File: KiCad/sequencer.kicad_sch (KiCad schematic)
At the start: 19 parts, among them J1 GATE OUT, J2 GATE OUT, J3 GATE OUT, Q1 BC548, U1 TL074

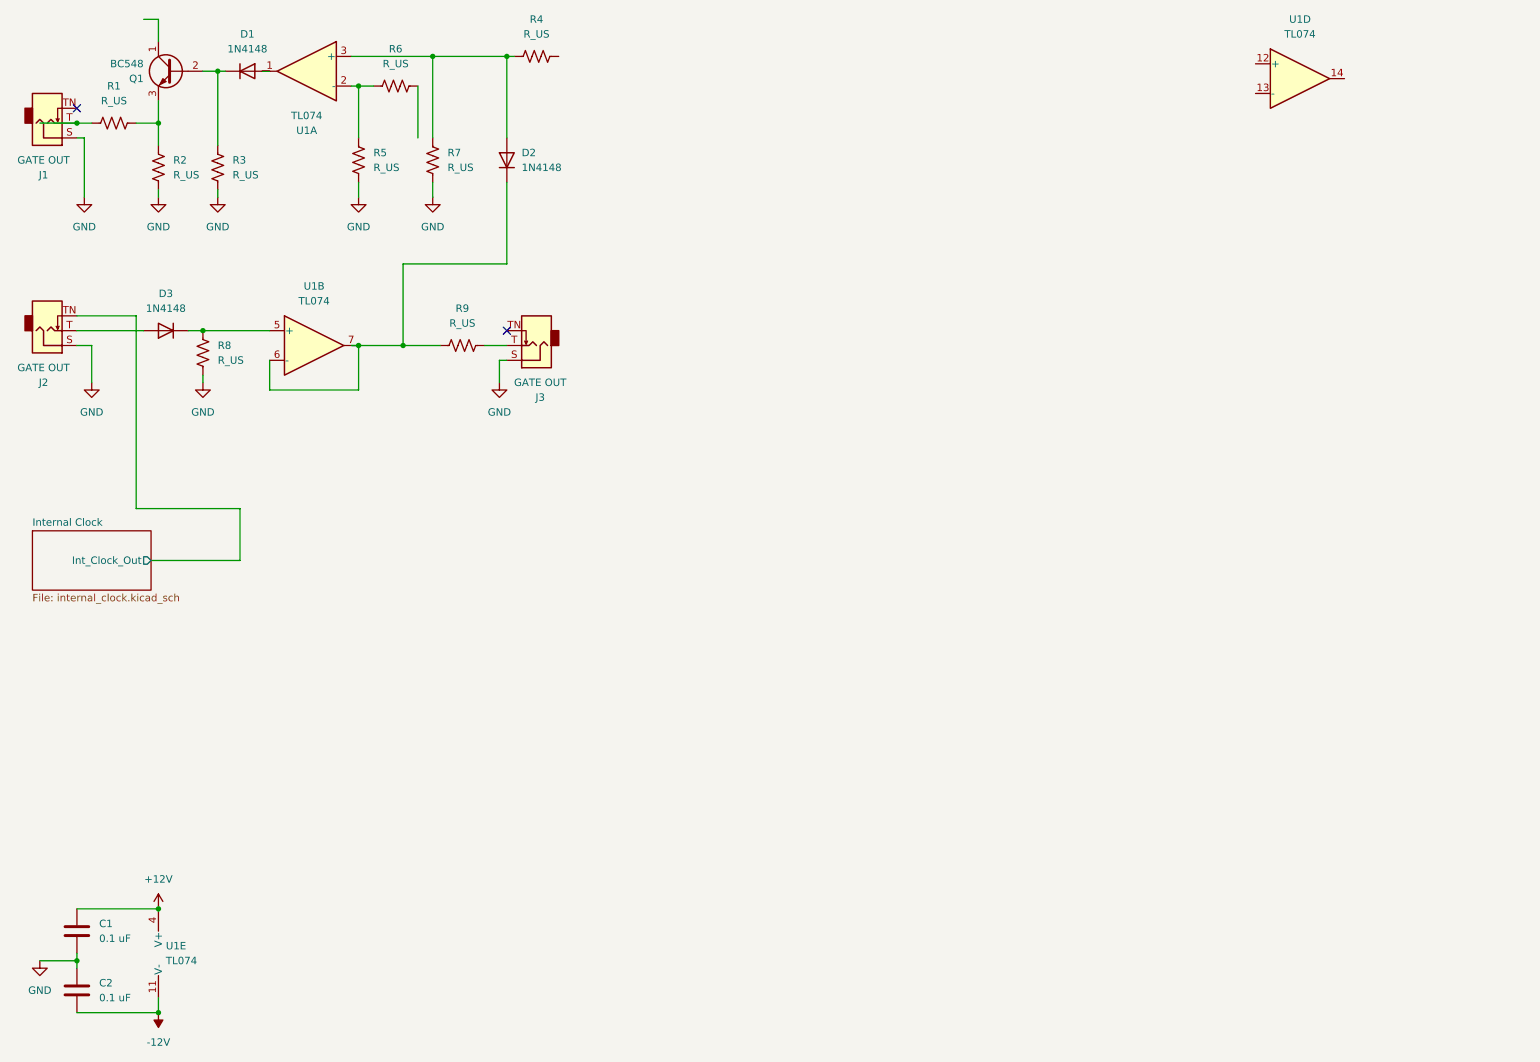
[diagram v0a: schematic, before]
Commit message: schematic: update cicada schematic
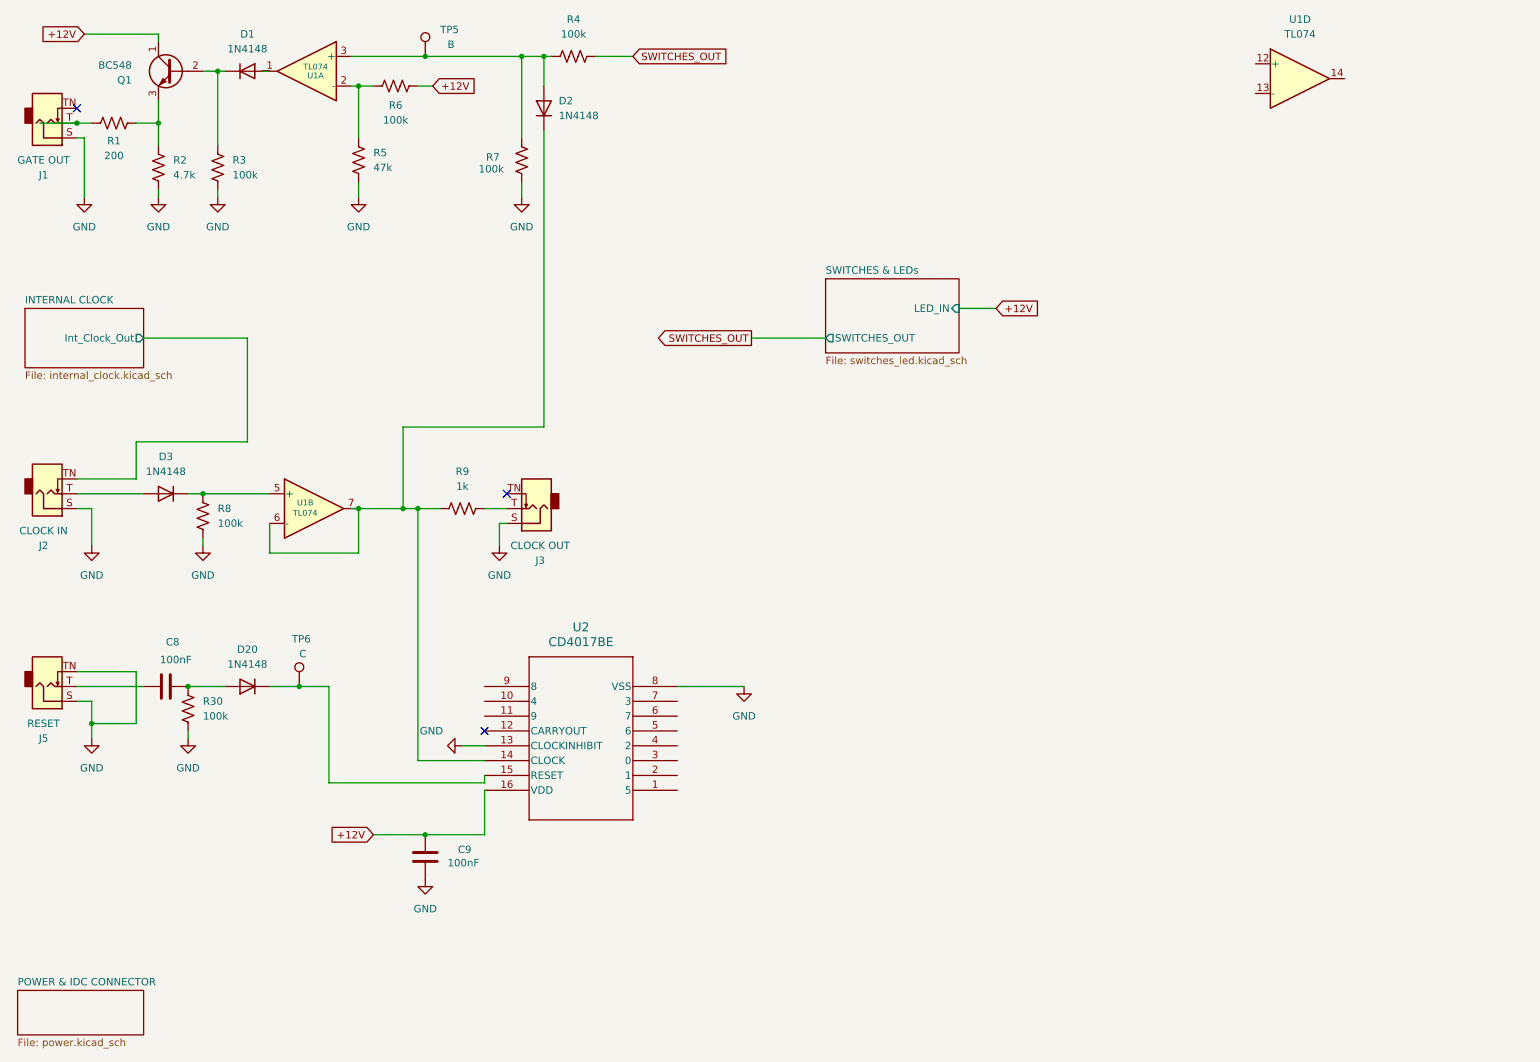
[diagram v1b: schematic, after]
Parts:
- removed C1, C2: 0.1 uF, symbol Device:C
- removed unit 5 of U1
- added C8, C9: 100nF, Capacitor_SMD:C_0805_2012Metric_Pad1.18x1.45mm_HandSolder, symbol Device:C
- added D20: 1N4148, Diode_THT:D_DO-35_SOD27_P7.62mm_Horizontal, symbol Diode:1N4148
- added J5: RESET, symbol Connector_Audio:AudioJack2_SwitchT
- added R30: 100k, symbol Device:R_US
- added TP5: B, symbol Connector:TestPoint
- added TP6: C, symbol Connector:TestPoint
- added U2: CD4017BE, N16, symbol Eurorack:CD4017BE
- J2: value GATE OUT -> CLOCK IN
- J3: value GATE OUT -> CLOCK OUT
- R1: value R_US -> 200
- R2: value R_US -> 4.7k
- R3, R4, R6, R7, R8: value R_US -> 100k
- R5: value R_US -> 47k
- R9: value R_US -> 1k
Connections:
- net +12V: now also Q1.1 (C), R6.1, C9.1, U2.16 (VDD)
- net GND: now also C9.2, J5.S, J5.TN, R30.1, U2.13 (CLOCKINHIBIT), U2.8 (VSS)
- net at D2.2 (A), R4.2, R7.2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: now also TP5.1
- net at D2.1 (K), R9.2, U1.6 (-)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: now also U2.14 (CLOCK)
- net SWITCHES_OUT: now reaches R4.1
- new net: D20.1 (K), TP6.1, U2.15 (RESET)
- new net: C8.1, D20.2 (A), R30.2
- new net: C8.2, J5.T
- no-connect marks 2 -> 3
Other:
- sheet Internal Clock renamed INTERNAL CLOCK
- added sheet POWER & IDC CONNECTOR (power.kicad_sch)
- added sheet SWITCHES & LEDs (switches_led.kicad_sch)
- moved on the sheet: D2, D3, J2, J3, R4, R7, R8, R9, U1B

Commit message: refactor(kicad): move switch/LED driver logic into switches_led sheet
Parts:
- removed U2: CD4017BE, N16, symbol Eurorack:CD4017BE
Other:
- sheet SWITCHES & LEDs ports: added none; removed LED_IN
- moved on the sheet: U1D
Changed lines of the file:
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@@
 	(wire
 		(pts
-			(xy 132.08 130.81) (xy 143.51 130.81)
+			(xy 109.22 86.36) (xy 109.22 35.56)
 		)
 		(stroke
@@
 	(wire
 		(pts
-			(xy 109.22 86.36) (xy 109.22 35.56)
+			(xy 105.41 22.86) (xy 105.41 36.83)
 		)
 		(stroke
@@
 	(wire
 		(pts
-			(xy 105.41 22.86) (xy 105.41 36.83)
+			(xy 31.75 137.16) (xy 39.37 137.16)
 		)
 		(stroke
@@
 	(wire
 		(pts
-			(xy 31.75 137.16) (xy 39.37 137.16)
+			(xy 30.48 46.99) (xy 30.48 36.83)
 		)
 		(stroke
@@
 	(wire
 		(pts
-			(xy 30.48 46.99) (xy 30.48 36.83)
+			(xy 29.21 95.25) (xy 39.37 95.25)
 		)
 		(stroke
@@
 	(wire
 		(pts
-			(xy 29.21 95.25) (xy 39.37 95.25)
+			(xy 175.26 151.13) (xy 177.8 151.13)
 		)
 		(stroke
@@
 	(wire
 		(pts
-			(xy 180.34 66.04) (xy 186.69 66.04)
-		)
-		(stroke
-			(width 0)
-			(type default)
-		)
-	)
-	(wire
-		(pts
 			(xy 85.09 100.33) (xy 85.09 86.36)
 		)
@@
 	(wire
 		(pts
-			(xy 144.78 71.12) (xy 157.48 71.12)
-		)
-		(stroke
-			(width 0)
-			(type default)
-		)
-	)
-	(wire
-		(pts
 			(xy 77.47 100.33) (xy 85.09 100.33)
 		)
@@
 	(global_label "SWITCHES_OUT"
 		(shape output)
-		(at 144.78 71.12 180)
-		(fields_autoplaced yes)
-		(effects
-			(font
-				(size 1.27 1.27)
-			)
-			(justify right)
-		)
-		(property "Intersheetrefs" "${INTERSHEET_REFS}"
-			(at 128.0063 71.12 0)
-			(effects
-				(font
-					(size 1.27 1.27)
-				)
-				(justify right)
-			)
-		)
-	)
-	(global_label "+12V"
-		(shape input)
-		(at 186.69 66.04 0)
+		(at 177.8 151.13 0)
 		(fields_autoplaced yes)
 		(effects
@@
 		)
 		(property "Intersheetrefs" "${INTERSHEET_REFS}"
-			(at 194.7552 66.04 0)
+			(at 194.5737 151.13 0)
 			(effects
 				(font
@@
 	)
 	(symbol
-		(lib_id "Eurorack:CD4017BE")
-		(at 132.08 148.59 180)
-		(unit 1)
-		(exclude_from_sim no)
-		(in_bom yes)
-		(on_board yes)
-		(dnp no)
-		(property "Reference" "U2"
-			(at 115.57 120.65 0)
-			(effects
-				(font
-					(size 1.524 1.524)
-				)
-			)
-		)
-		(property "Value" "CD4017BE"
-			(at 115.57 123.19 0)
-			(effects
-				(font
-					(size 1.524 1.524)
-				)
-			)
-		)
-		(property "Footprint" "N16"
-			(at 132.08 148.59 0)
-			(effects
-				(font
-					(size 1.27 1.27)
-					(italic yes)
-				)
-				(hide yes)
-			)
-		)
-		(property "Datasheet" "https://www.ti.com/lit/gpn/cd4017b"
-			(at 132.08 148.59 0)
-			(effects
-				(font
-					(size 1.27 1.27)
-					(italic yes)
-				)
-				(hide yes)
-			)
-		)
-		(property "Description" ""
-			(at 132.08 148.59 0)
-			(effects
-				(font
-					(size 1.27 1.27)
-				)
-				(hide yes)
-			)
-		)
-		(pin "11"
-		)
-		(pin "10"
-		)
-		(pin "9"
-		)
-		(pin "3"
-		)
-		(pin "12"
-		)
-		(pin "14"
-		)
-		(pin "13"
-		)
-		(pin "4"
-		)
-		(pin "1"
-		)
-		(pin "16"
-		)
-		(pin "6"
-		)
-		(pin "15"
-		)
-		(pin "8"
-		)
-		(pin "2"
-		)
-		(pin "7"
-		)
-		(pin "5"
-		)
-		(instances
-			(project ""
-				(path "/c997e785-a132-463f-bd08-a5a67a697207"
-					(reference "U2")
-					(unit 1)
-				)
-			)
-		)
-	)
-	(symbol
 		(lib_id "Amplifier_Operational:TL074")
 		(at 68.58 25.4 0)
@@
 	(symbol
 		(lib_id "Amplifier_Operational:TL074")
-		(at 238.76 26.67 0)
+		(at 232.41 148.59 0)
 		(unit 4)
 		(exclude_from_sim no)
@@
 		(fields_autoplaced yes)
 		(property "Reference" "U1"
-			(at 238.76 16.51 0)
+			(at 232.41 138.43 0)
 			(effects
 				(font
@@
 		)
 		(property "Value" "TL074"
-			(at 238.76 19.05 0)
+			(at 232.41 140.97 0)
 			(effects
 				(font
@@
 		)
 		(property "Footprint" ""
-			(at 237.49 24.13 0)
+			(at 231.14 146.05 0)
 			(effects
 				(font
@@
 		)
 		(property "Datasheet" "http://www.ti.com/lit/ds/symlink/tl071.pdf"
-			(at 240.03 21.59 0)
+			(at 233.68 143.51 0)
 			(effects
 				(font
@@
 		)
 		(property "Description" "Quad Low-Noise JFET-Input Operational Amplifiers, DIP-14/SOIC-14"
-			(at 238.76 26.67 0)
+			(at 232.41 148.59 0)
 			(effects
 				(font
@@
 	(symbol
 		(lib_id "power:GND")
-		(at 143.51 130.81 0)
-		(unit 1)
-		(exclude_from_sim no)
-		(in_bom yes)
-		(on_board yes)
-		(dnp no)
-		(fields_autoplaced yes)
-		(property "Reference" "#PWR024"
-			(at 143.51 137.16 0)
-			(effects
-				(font
-					(size 1.27 1.27)
-				)
-				(hide yes)
-			)
-		)
-		(property "Value" "GND"
-			(at 143.51 135.89 0)
-			(effects
-				(font
-					(size 1.27 1.27)
-				)
-			)
-		)
-		(property "Footprint" ""
-			(at 143.51 130.81 0)
-			(effects
-				(font
-					(size 1.27 1.27)
-				)
-				(hide yes)
-			)
-		)
-		(property "Datasheet" ""
-			(at 143.51 130.81 0)
-			(effects
-				(font
-					(size 1.27 1.27)
-				)
-				(hide yes)
-			)
-		)
-		(property "Description" "Power symbol creates a global label with name \"GND\" , ground"
-			(at 143.51 130.81 0)
-			(effects
-				(font
-					(size 1.27 1.27)
-				)
-				(hide yes)
-			)
-		)
-		(pin "1"
-		)
-		(instances
-			(project "sequencer"
-				(path "/c997e785-a132-463f-bd08-a5a67a697207"
-					(reference "#PWR024")
-					(unit 1)
-				)
-			)
-		)
-	)
-	(symbol
-		(lib_id "power:GND")
 		(at 88.9 163.83 0)
 		(unit 1)
@@
 	)
 	(sheet
-		(at 157.48 60.96)
+		(at 152.4 148.59)
 		(size 22.86 12.7)
 		(exclude_from_sim no)
@@
 		)
 		(property "Sheetname" "SWITCHES & LEDs"
-			(at 157.48 60.2484 0)
+			(at 152.4 147.8784 0)
 			(effects
 				(font
@@
 		)
 		(property "Sheetfile" "switches_led.kicad_sch"
-			(at 157.48 74.2446 0)
+			(at 152.4 161.8746 0)
 			(effects
 				(font
@@
 		)
 		(pin "SWITCHES_OUT" output
-			(at 157.48 71.12 180)
-			(effects
-				(font
-					(size 1.27 1.27)
-				)
-				(justify left)
-			)
-		)
-		(pin "LED_IN" input
-			(at 180.34 66.04 0)
+			(at 175.26 151.13 0)
 			(effects
 				(font

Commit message: refactor(kicad): finishing root
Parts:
- removed C9: 100nF, Capacitor_SMD:C_0805_2012Metric_Pad1.18x1.45mm_HandSolder, symbol Device:C
- removed J3: CLOCK OUT, symbol Connector_Audio:AudioJack2_SwitchT
- added J6: CV OUT, symbol Connector_Audio:AudioJack2_SwitchT
- added J7: CLOCK OUT, symbol Connector_Audio:AudioJack2_SwitchT
- added R32, R33, R34: 1k, symbol Device:R_US
- added R35: 100k, symbol Device:R_US
- added RV10, RV11: R_Potentiometer_Trim_US, symbol Device:R_Potentiometer_Trim_US
- added SW10: SW_Nidec_CAS-120A1, Button_Switch_SMD:Nidec_Copal_CAS-120A, symbol Switch:SW_Nidec_CAS-120A1
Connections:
- net GND: now also J6.S, J7.S, R33.1, R34.1, RV10.1, RV10.3, RV11.1, RV11.3
- net CLOCK OUT: now reaches R9.1
- net CLOCK OUT: now also J7.T
- net SWITCHES & LEDs/EXTERNAL RESET: now reaches D20.1 (K), TP6.1
- net at U1.12 (+): now also R35.2, SW10.2 (B)
- net at U1.13 (-): now also U1.14, R32.2
- net SWITCHES & LEDs/EXTERNAL CLOCK: now reaches D2.1 (K), R9.2, U1.6 (-), U1.7
- net SWITCHES_OUT renamed SWITCHES & LEDs/GATE OUT
- new net: R33.2, SW10.1 (C)
- new net: R34.2, SW10.3 (A)
- new net: J6.T, R32.1
- new net SWITCHES & LEDs/CV OUT: R35.1
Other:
- sheet SWITCHES & LEDs ports: added CV OUT, EXTERNAL CLOCK, EXTERNAL RESET, GATE OUT; removed SWITCHES_OUT
- moved on the sheet: D1, D2, J1, Q1, R1, R2, R3, R4, R5, R6, R7, TP5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
